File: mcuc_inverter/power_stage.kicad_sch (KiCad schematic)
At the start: 0 parts

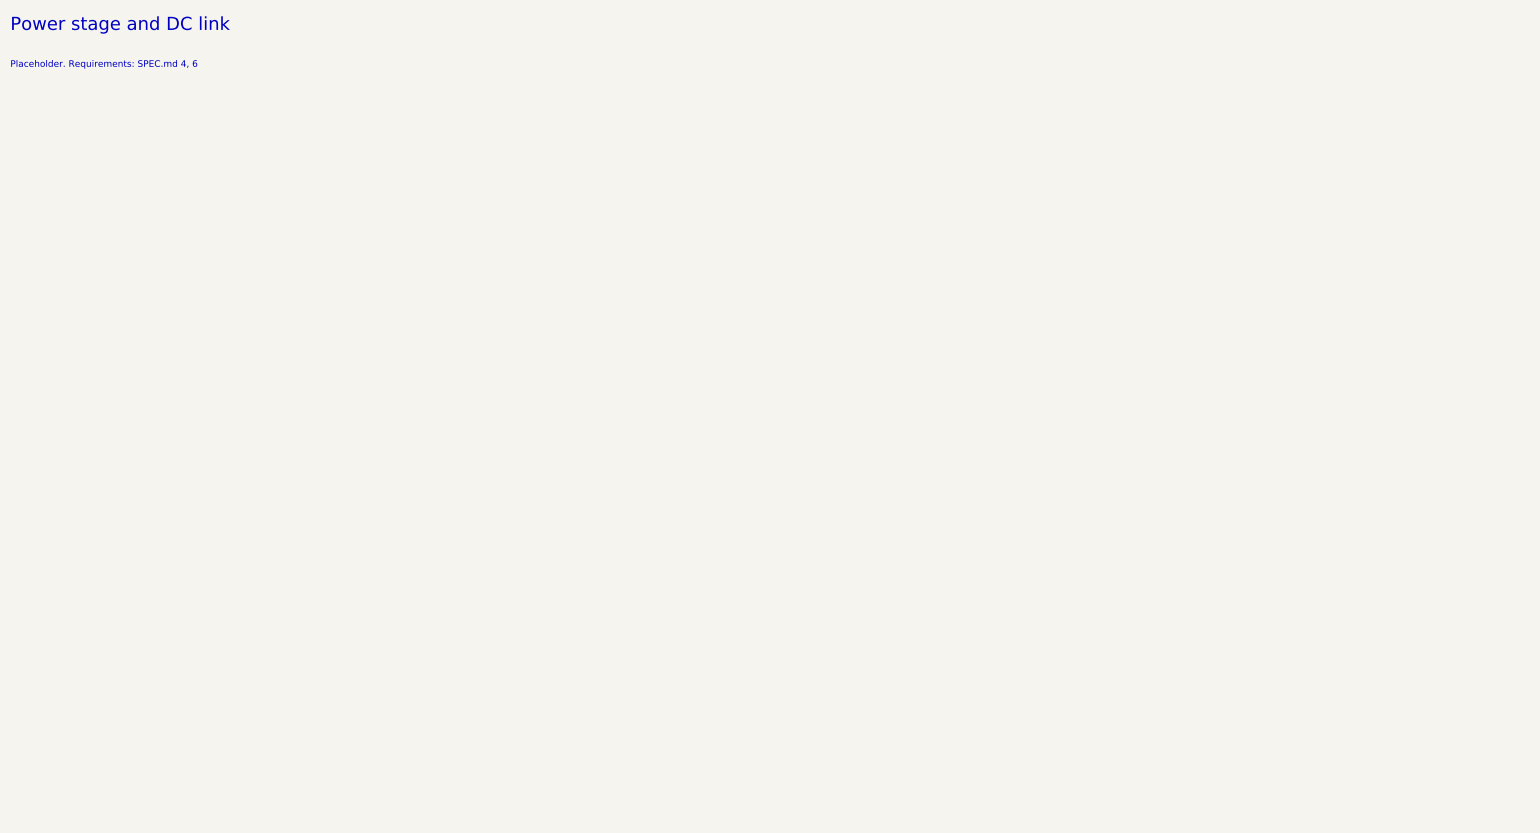
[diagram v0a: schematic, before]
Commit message: Capture power_stage sheet: FS02MR12A8MA2B module + DC-link bank
Custom symbol (project lib mcuc_inverter.kicad_sym) built from the
module datasheet pin map, Fig. 1/3/4: 39 pins - G1-G6, dual Kelvin
sources S1.1..S6.2, drain-sense D1-D6, TS1-TS3 diode pairs, and 9
power terminals (P1-3/N1-3/U/V/W, per-phase DC feeds tied on-sheet,
laminated busbar note). Switch mapping odd=HS/even=LS, 1/2=U 3/4=V
5/6=W per Fig. 1.

DC-link: C201-C205, 5x 100uF 900V film [TBV], with the SPEC 6.1 bank
duty note (>=400uF, >=80 A rms @ 70C, 114 A/120 s TBV) and the
AN-G2-ASSEMBLY PressFIT pattern note.

ERC 0 errors; netlist assertion 49 pins / 29 nets, 0 mismatches.

Co-Authored-By: Claude Fable 5 <noreply@anthropic.com>
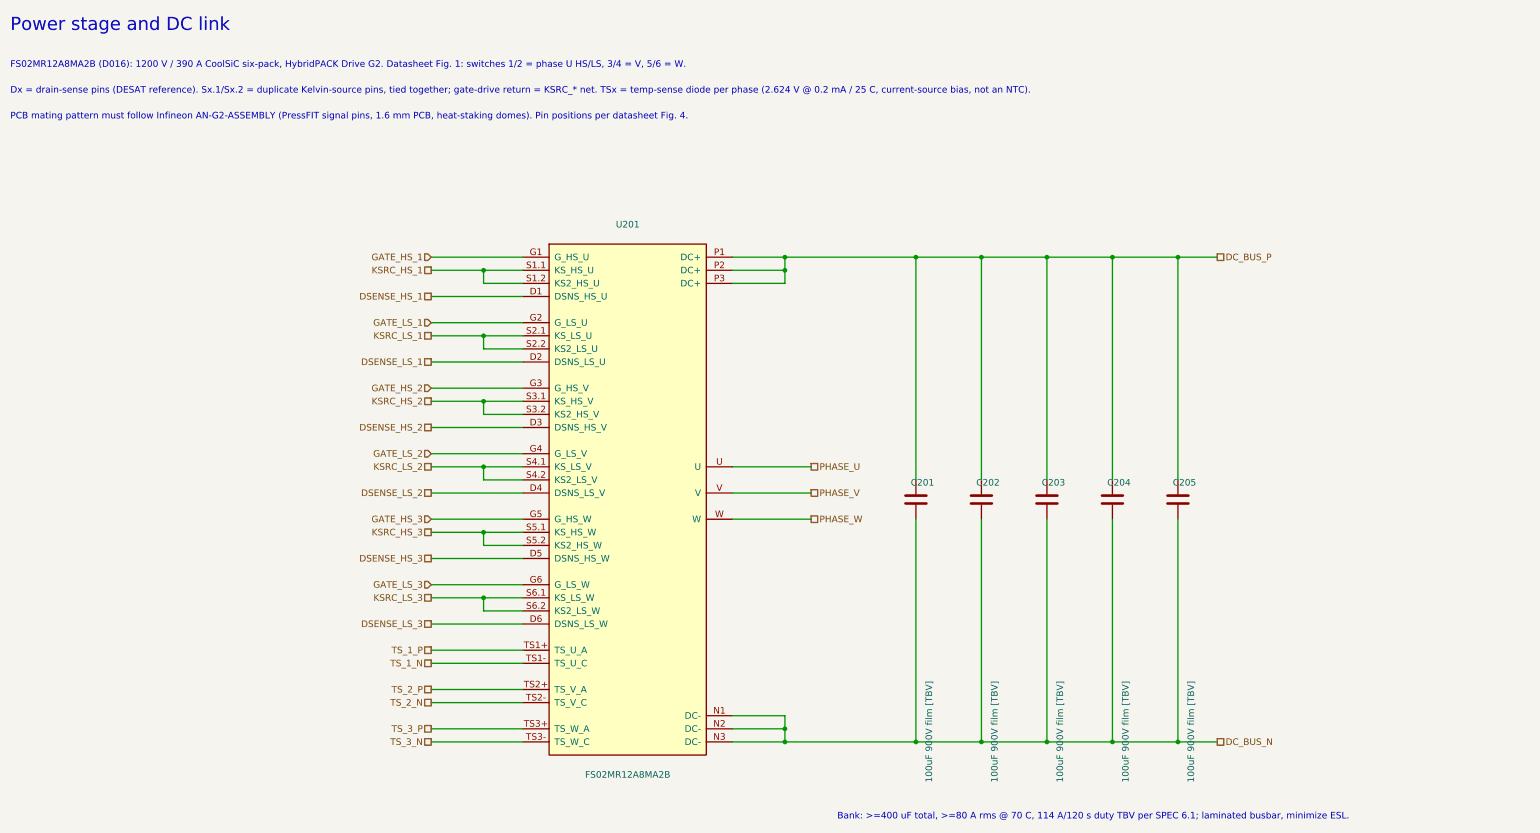
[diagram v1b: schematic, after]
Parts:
- added C201, C202, C203, C204, C205: 100uF 900V film [TBV], symbol Device:C
- added U201: FS02MR12A8MA2B, symbol mcuc:FS02MR12A8MA2B
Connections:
- new net DC_BUS_N: C201.2, C202.2, C203.2, C204.2, C205.2, U201.N1 (DC-), U201.N2 (DC-), U201.N3 (DC-)
- new net DC_BUS_P: C201.1, C202.1, C203.1, C204.1, C205.1, U201.P1 (DC+), U201.P2 (DC+), U201.P3 (DC+)
- new net DSENSE_HS_1: U201.D1 (DSNS_HS_U)
- new net DSENSE_HS_2: U201.D3 (DSNS_HS_V)
- new net DSENSE_HS_3: U201.D5 (DSNS_HS_W)
- new net DSENSE_LS_1: U201.D2 (DSNS_LS_U)
- new net DSENSE_LS_2: U201.D4 (DSNS_LS_V)
- new net DSENSE_LS_3: U201.D6 (DSNS_LS_W)
- new net GATE_HS_1: U201.G1 (G_HS_U)
- new net GATE_HS_2: U201.G3 (G_HS_V)
- new net GATE_HS_3: U201.G5 (G_HS_W)
- new net GATE_LS_1: U201.G2 (G_LS_U)
- new net GATE_LS_2: U201.G4 (G_LS_V)
- new net GATE_LS_3: U201.G6 (G_LS_W)
- new net KSRC_HS_1: U201.S1.1 (KS_HS_U), U201.S1.2 (KS2_HS_U)
- new net KSRC_HS_2: U201.S3.1 (KS_HS_V), U201.S3.2 (KS2_HS_V)
- new net KSRC_HS_3: U201.S5.1 (KS_HS_W), U201.S5.2 (KS2_HS_W)
- new net KSRC_LS_1: U201.S2.1 (KS_LS_U), U201.S2.2 (KS2_LS_U)
- new net KSRC_LS_2: U201.S4.1 (KS_LS_V), U201.S4.2 (KS2_LS_V)
- new net KSRC_LS_3: U201.S6.1 (KS_LS_W), U201.S6.2 (KS2_LS_W)
- new net PHASE_U: U201.U
- new net PHASE_V: U201.V
- new net PHASE_W: U201.W
- new net TS_1_N: U201.TS1- (TS_U_C)
- new net TS_1_P: U201.TS1+ (TS_U_A)
- new net TS_2_N: U201.TS2- (TS_V_C)
- new net TS_2_P: U201.TS2+ (TS_V_A)
- new net TS_3_N: U201.TS3- (TS_W_C)
- new net TS_3_P: U201.TS3+ (TS_W_A)
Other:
- note added: "Bank: >=400 uF total, >=80 A rms @ 70 C, 114 A/120 s duty TBV per SPEC 6.1; laminated busbar, minimize ESL."
- note added: "Dx = drain-sense pins (DESAT reference). Sx.1/Sx.2 = duplicate Kelvin-source pins, tied together; gate-drive return = KSRC_* net. TSx = temp-sense diode per phase (2.624 V @ 0.2 mA / 25 C, current-source bias, not an NTC)."
- note added: "FS02MR12A8MA2B (D016): 1200 V / 390 A CoolSiC six-pack, HybridPACK Drive G2. Datasheet Fig. 1: switches 1/2 = phase U HS/LS, 3/4 = V, 5/6 = W."
- note added: "PCB mating pattern must follow Infineon AN-G2-ASSEMBLY (PressFIT signal pins, 1.6 mm PCB, heat-staking domes). Pin positions per datasheet Fig. 4."
- note removed: "Placeholder. Requirements: SPEC.md 4, 6"

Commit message: Board-prep: footprint audit complete, HV terminals, off-board flags
474-component audit: 466 valid resolved footprints, 13 off-board
exclusions per D024 (caps to carrier, chassis resistors, HOYS), 4
flagged TBDs (custom flyback + 3 unchosen inductors), zero silent
gaps. Netlist-fatal fixes: Q403 renumbered to Wolfspeed TO-263-7
convention (G1/KS2/S3-7/tab-D8), CSD18543Q3A remapped to KiCad's
SSSGD VSON-8 pairing - both verified in the netlist afterward.

New HV interface terminals J401-J405 (M4 ring-lug pads: DC input,
precharge-R chassis loop, discharge-R return, bus taps) and HOYS
harness headers J501-J503 (JST 2mm; PA-vs-PH footprint flagged TBV)
with net membership machine-verified incl. the OC_TRIP wire-OR and
I_REF paths to the MCU ADCs.

ERC 0 errors, warnings 201 -> 200 (none introduced).

Co-Authored-By: Claude Fable 5 <noreply@anthropic.com>
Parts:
- C201, C202, C203, C204, C205: footprint (none) -> mcuc:MKP1848C_6pin_52.5x20.3
- U201: footprint (none) -> mcuc:FS02MR12A8MA2B_PressFIT
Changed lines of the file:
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@@
 			)
 		)
-		(property "Footprint" ""
+		(property "Footprint" "mcuc:FS02MR12A8MA2B_PressFIT"
 			(at 139.7 109.22 0)
 			(effects
@@
 		(exclude_from_sim no)
 		(in_bom yes)
-		(on_board yes)
+		(on_board no)
 		(dnp no)
 		(property "Reference" "C201"
@@
 			)
 		)
-		(property "Footprint" ""
+		(property "Footprint" "mcuc:MKP1848C_6pin_52.5x20.3"
 			(at 195.58 110.49 0)
 			(effects
@@
 		(exclude_from_sim no)
 		(in_bom yes)
-		(on_board yes)
+		(on_board no)
 		(dnp no)
 		(property "Reference" "C202"
@@
 			)
 		)
-		(property "Footprint" ""
+		(property "Footprint" "mcuc:MKP1848C_6pin_52.5x20.3"
 			(at 208.28 110.49 0)
 			(effects
@@
 		(exclude_from_sim no)
 		(in_bom yes)
-		(on_board yes)
+		(on_board no)
 		(dnp no)
 		(property "Reference" "C203"
@@
 			)
 		)
-		(property "Footprint" ""
+		(property "Footprint" "mcuc:MKP1848C_6pin_52.5x20.3"
 			(at 220.98 110.49 0)
 			(effects
@@
 		(exclude_from_sim no)
 		(in_bom yes)
-		(on_board yes)
+		(on_board no)
 		(dnp no)
 		(property "Reference" "C204"
@@
 			)
 		)
-		(property "Footprint" ""
+		(property "Footprint" "mcuc:MKP1848C_6pin_52.5x20.3"
 			(at 233.68 110.49 0)
 			(effects
@@
 		(exclude_from_sim no)
 		(in_bom yes)
-		(on_board yes)
+		(on_board no)
 		(dnp no)
 		(property "Reference" "C205"
@@
 			)
 		)
-		(property "Footprint" ""
+		(property "Footprint" "mcuc:MKP1848C_6pin_52.5x20.3"
 			(at 246.38 110.49 0)
 			(effects
